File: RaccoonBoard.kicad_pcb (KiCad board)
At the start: 4 copper layers, 59.1 x 92.7 mm, 106 parts, among them J1 BOOT SD, J2 USB_A, J3 USB_A, J4 UART0, J5 IO1, J6 IO2, J7 HR911105A, P1 USB PWR, SW1 RST, U1 NUC980DK61Y, U3 LAN8720A, U4 AP1117-33, U5 AZ1117-1.2, U6 LP2985-1.8, Y1 32K, Y2 12MHz, Y3 25MHz

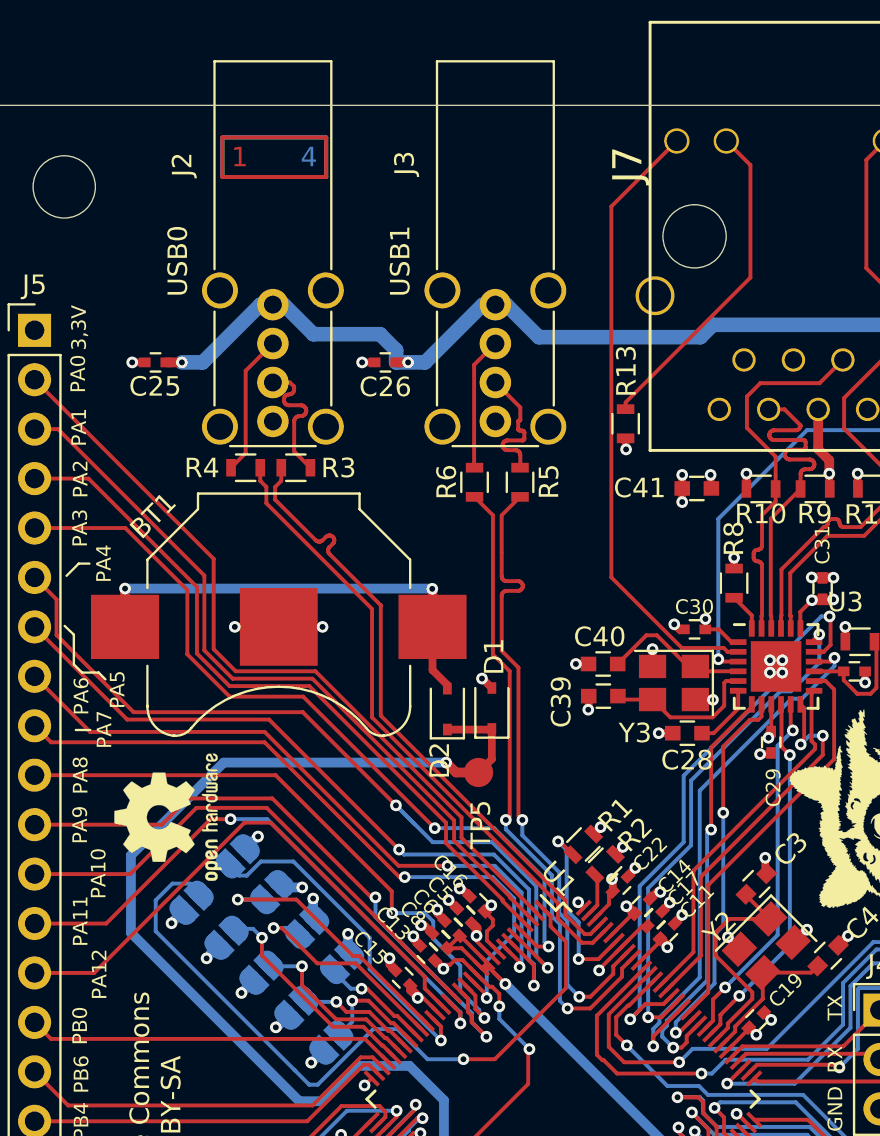
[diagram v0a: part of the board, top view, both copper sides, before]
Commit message: Improved USB and ETH routing (matched lengths/skew)
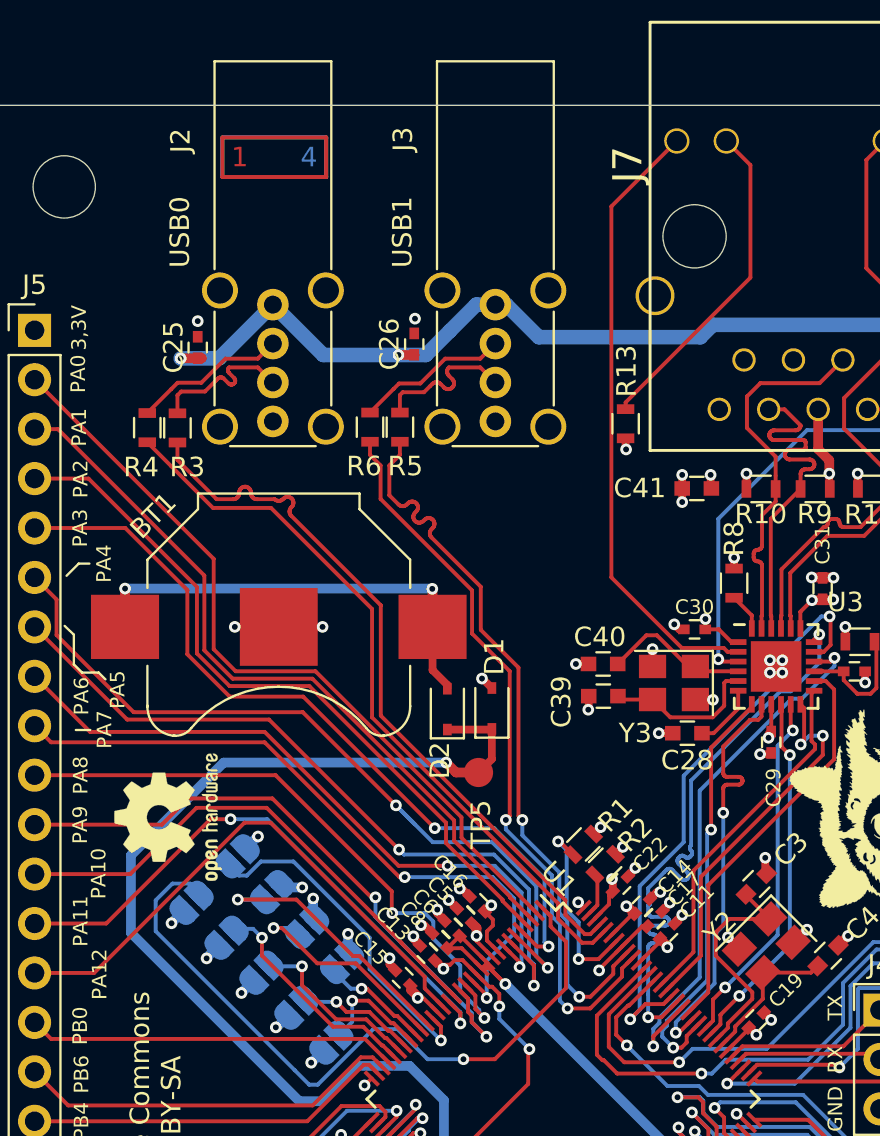
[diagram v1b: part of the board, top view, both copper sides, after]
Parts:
- moved R5 6.79 mm to (135.1, 69.2)
- moved R3 6.42 mm to (123.7, 69.3), turned to 270 degrees
- moved R6 6.07 mm to (133.6, 69.2)
- moved R4 5.46 mm to (122.1, 69.3), turned to 270 degrees
- moved C25 2.30 mm to (124.7, 65.1), turned to 90 degrees
- moved C26 1.75 mm to (135.8, 65.0), turned to 90 degrees
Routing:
- net USB0D_P: track 32.7 -> 38.2 mm
- net USB0D_N: track 32.7 -> 38.2 mm
- net USB1D_P: track 33.1 -> 38.2 mm
- net USB1D_N: track 33.1 -> 38.2 mm
- net ETH_TXD1: track 26.3 -> 30.9 mm
- net ETH_RXD0: track 20.2 -> 21.8 mm
- net GND: track 75.6 -> 74.3 mm
- net /D1-: track 6.84 -> 7.91 mm
- net /D1+: track 6.88 -> 7.91 mm
- net /D0-: track 7.27 -> 7.93 mm
- net /D0+: track 8.01 -> 8.66 mm

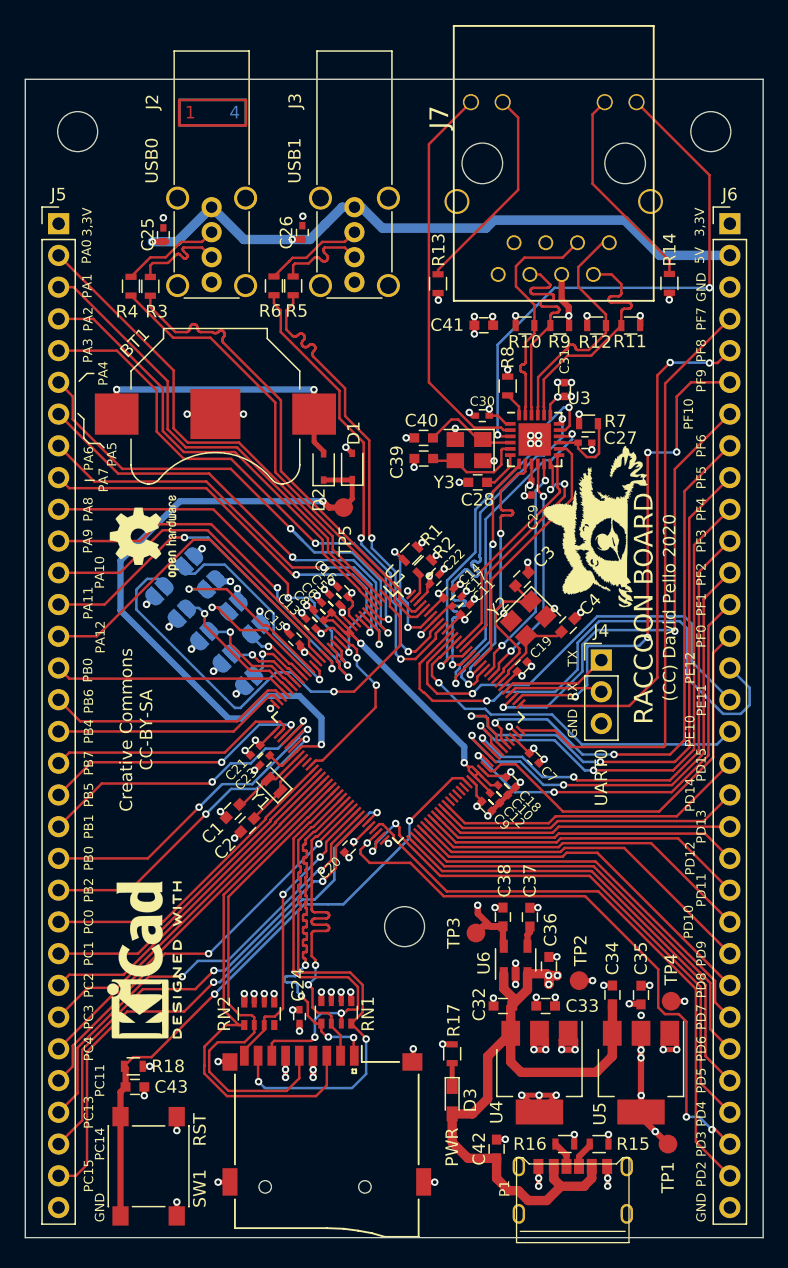
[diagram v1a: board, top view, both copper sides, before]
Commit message: Updated to lastest KiCAD libraries, improved silkscreens, small fixes to routing
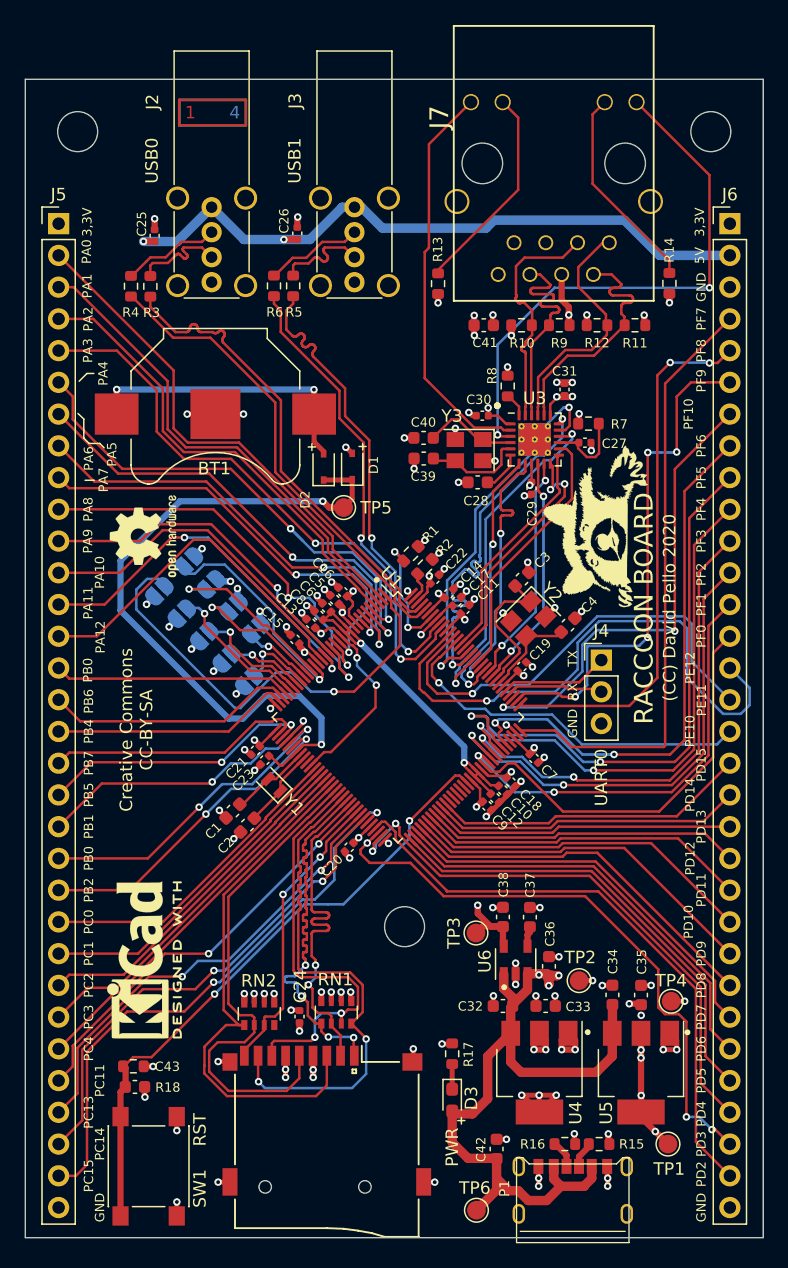
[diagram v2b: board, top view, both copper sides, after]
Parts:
- added TP6: VIN, TestPoint:TestPoint_Pad_D1.5mm, F.Cu at (149.8, 143.2)
- C1, C2, C28, C3, C32, C33, C34, C35, C36, C37, C38, C39, C4, C40, C41, C42, C43: footprint Capacitors_SMD:C_0603 -> Capacitor_SMD:C_0603_1608Metric
- C10, C11, C12, C13, C14, C15, C16, C17, C18, C19, C20, C21, C22, C23, C24, C25, C26, C27, C29, C30, C31, C5, C6, C7, C8, C9: footprint Capacitors_SMD:C_0402 -> Capacitor_SMD:C_0402_1005Metric
- D1, D2: footprint Diodes_SMD:D_SOD-323 -> Diode_SMD:D_SOD-323
- D3: footprint LEDs:LED_0603_HandSoldering -> LED_SMD:LED_0603_1608Metric_Pad1.05x0.95mm_HandSolder
- J4: footprint Pin_Headers:Pin_Header_Straight_1x03_Pitch2.54mm -> Connector_PinHeader_2.54mm:PinHeader_1x03_P2.54mm_Vertical
- J5, J6: footprint Pin_Headers:Pin_Header_Straight_1x32_Pitch2.54mm -> Connector_PinHeader_2.54mm:PinHeader_1x32_P2.54mm_Vertical
- JP1, JP2, JP3, JP4, JP5, JP6, JP7, JP8, JP9: footprint Jumpers:SolderJumper-2_P1.3mm_Open_RoundedPad1.0x1.5mm -> Jumper:SolderJumper-2_P1.3mm_Open_RoundedPad1.0x1.5mm
- R1, R10, R11, R12, R13, R14, R15, R16, R17, R18, R2, R3, R4, R5, R6, R7, R8, R9: footprint Resistors_SMD:R_0603 -> Resistor_SMD:R_0603_1608Metric
- RN1, RN2: footprint Resistors_SMD:R_Array_Convex_4x0603 -> Resistor_SMD:R_Array_Convex_4x0603
- TP1, TP2, TP3, TP4, TP5: footprint Measurement_Points:Measurement_Point_Round-SMD-Pad_Small -> TestPoint:TestPoint_Pad_D1.5mm
- U1: footprint Housings_QFP:LQFP-128_14x14mm_Pitch0.4mm -> Package_QFP:LQFP-128_14x14mm_P0.4mm
- U3: footprint Housings_DFN_QFN:QFN-24-1EP_4x4mm_Pitch0.5mm -> Package_DFN_QFN:QFN-24-1EP_4x4mm_P0.5mm_EP2.6x2.6mm_ThermalVias
- U4, U5: footprint TO_SOT_Packages_SMD:SOT-223-3_TabPin2 -> Package_TO_SOT_SMD:SOT-223-3_TabPin2
- U6: footprint TO_SOT_Packages_SMD:SOT-23-5 -> Package_TO_SOT_SMD:SOT-23-5
- Y1: footprint Crystals:Crystal_SMD_2012-2pin_2.0x1.2mm -> Crystal:Crystal_SMD_2012-2Pin_2.0x1.2mm
- Y2, Y3: footprint Crystals:Crystal_SMD_3225-4pin_3.2x2.5mm -> Crystal:Crystal_SMD_3225-4Pin_3.2x2.5mm
- moved C25 0.70 mm to (124.0, 65.2)
- moved C26 0.41 mm to (135.4, 65.0)
- moved R11 0.34 mm to (162.5, 72.4)
- moved R10 0.28 mm to (153.4, 72.4)
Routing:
- net +3V3: track 60.4 -> 65.0 mm
- net +5V: track 205.5 -> 209.3 mm
- net GND: track 74.3 -> 76.6 mm, vias 92 -> 88
- net +1V2: track 115.1 -> 116.5 mm
- net +1V8: track 48.1 -> 49.3 mm
- net +BATT: track 57.3 -> 58.5 mm
- net UART0RX: track 7.60 -> 8.76 mm
- net PB7: track 20.4 -> 21.4 mm
- net PD2: track 47.6 -> 48.6 mm
- net PF9: track 40.7 -> 41.7 mm
- net Net-(R2-Pad1): track 2.20 -> 3.14 mm
- net Net-(JP6-Pad1): track 17.5 -> 18.3 mm
- net PB4: track 19.0 -> 19.7 mm
- net PF0: track 32.2 -> 33.0 mm
- net PF6: track 44.1 -> 44.8 mm
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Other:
- net class Default: clearance 0.18 -> 0.1524
- rule trace_clearance: 0.18 -> 0.1524
